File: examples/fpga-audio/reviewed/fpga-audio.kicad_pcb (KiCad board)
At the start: 2 copper layers, 100 x 84 mm, 29 parts, among them J1 3V3 IN, J2 AUDIO OUT, J3 SPI PROG, U1 iCE40UP5K, U2 PCM5102A, U3 AP2112K-1.2, U4 W25Q32JV, X1 12MHz

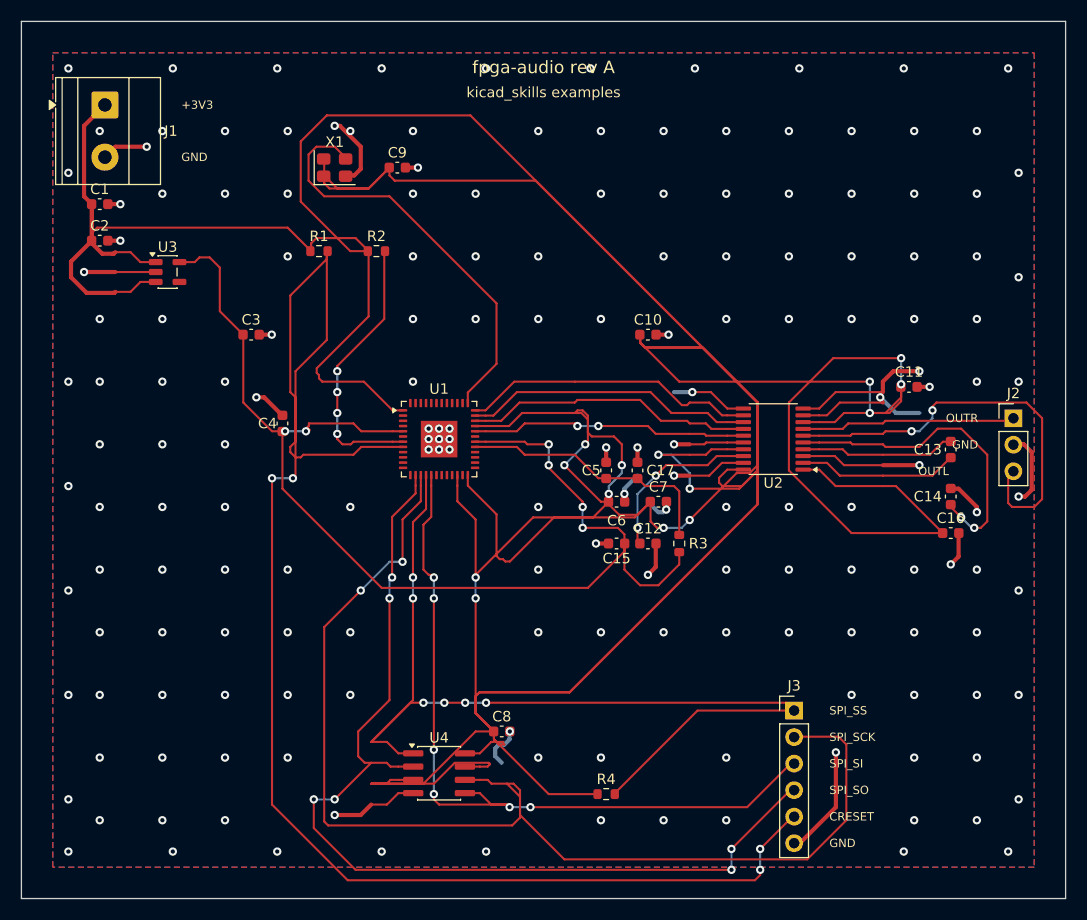
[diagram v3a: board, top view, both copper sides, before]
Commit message: Learn the drawing from the boards people drew
The brief for this round: relying on the autorouter and the numbers alone is
not enough - organise what pictorial correctness looks like from ordinary
circuits and open designs, and improve the drawing itself. So it starts in
KiCad's own demo corpus, measured and looked at, and ends with the habits
pushed into the generator.

tools/board_signature.py (new) reduces "looks autorouted" to five numbers.
Hand-routed two-layer boards cluster tightly: 10-47% of copper on the second
face, median segments 1.8-3.5 mm, 9-25 corners per decimetre, 91-98% of them
45s, 0.3-16 vias per decimetre. Rendering interf_u beside our boards says the
same thing in one glance: a layer has a direction, a bus travels as a bundle,
a person covers an offset with the long straight and one diagonal.

Three habits, now in the generator:

* Router.route(follow=...): cells beside a sibling net's path are discounted,
  so a bus (nets sharing a name prefix - I2S_*, SPI_*) travels as parallel
  lanes in one corridor. The discount is a fraction of a step, so it never
  buys a detour.
* _doglegged: every wiggly stretch is redrawn as the human stroke - the
  straight along the dominant direction plus one 45 - when the dogleg is
  clear, recursing into halves where a crossing blocks the whole. The op-amp
  board's median segment rose from 0.75 mm and its corner rate fell from
  38/dm; the FPGA board landed at 1.54 mm and 17.8/dm, inside the human band.
* Purposeful stitching: the 6 mm via carpet is gone. A ring at the rim, vias
  beside every back-layer crossing (where the plane is actually cut), and a
  coarse 12 mm mesh so no pour orphans. Vias/dm: buck 41 -> 18, carrier
  28 -> 13, all five inside the corpus band, pour_fragmented still silent.

Three failures the round produced and what they taught:

* pinned(): reshaping may not move copper off any point inside an own-net
  pad - the centre alone was not enough, a routed run touches off-centre and
  the ove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
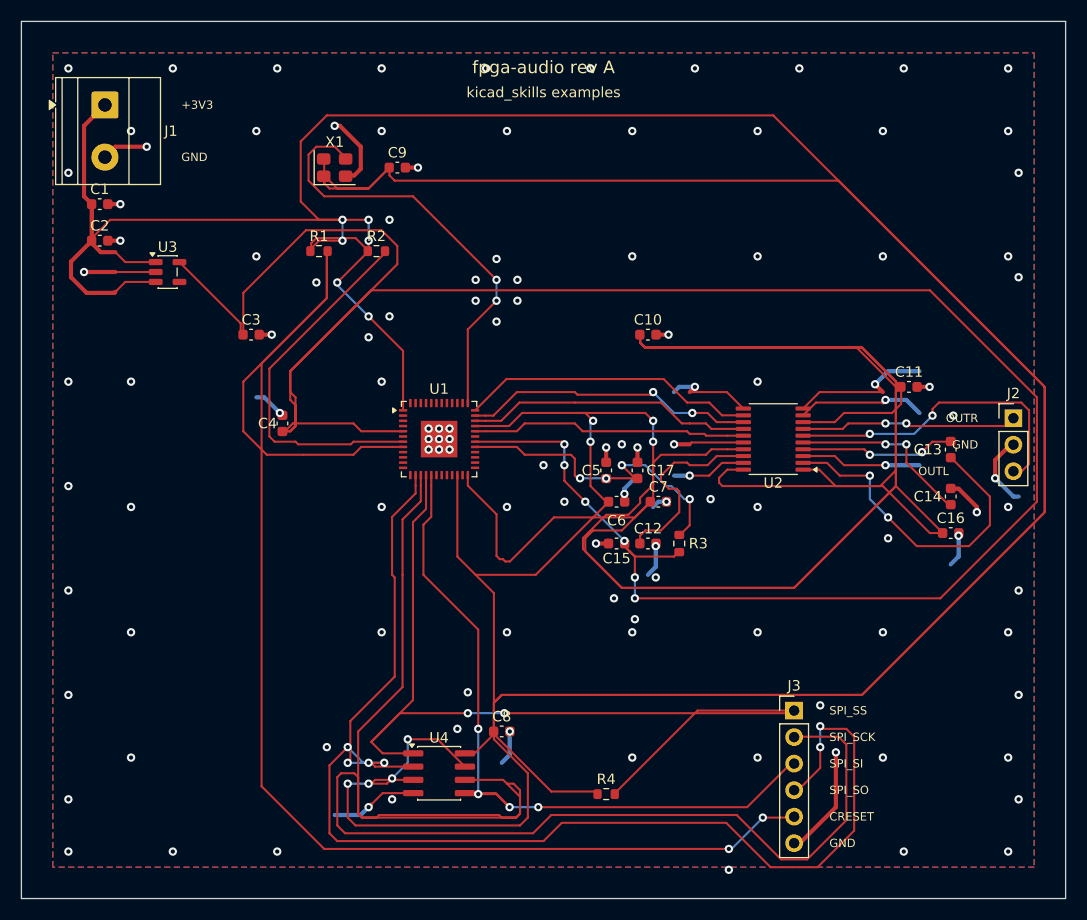
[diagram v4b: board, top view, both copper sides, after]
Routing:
- net +3V3: track 685.4 -> 905.9 mm
- net /+1V2: track 112.4 -> 237.2 mm
- net /SPI_SCK: track 115.9 -> 154.2 mm, vias 2 -> 0
- net /SPI_SO: track 96.7 -> 125.8 mm
- net /CAPP: track 15.4 -> 31.4 mm, vias 0 -> 2
- net /VNEG: track 30.8 -> 17.6 mm
- net /OUTL: track 40.2 -> 30.5 mm
- net /CDONE: track 26.5 -> 35.6 mm, vias 4 -> 0
- net /VCCPLL: track 25.5 -> 31.5 mm, vias 0 -> 4
- net /SPI_SI: track 73.2 -> 70.1 mm, vias 6 -> 4
- net /LDOO: track 16.5 -> 19.0 mm, vias 2 -> 0
- net /CLK12: track 40.5 -> 41.8 mm, vias 0 -> 2
- net /SPI_SS: track 95.1 -> 94.5 mm, vias 6 -> 2
- net /CRESET: track 146.0 -> 145.7 mm, vias 4 -> 2
- net GND: track 138.1 -> 137.8 mm, vias 177 -> 121
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
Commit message: A net may not cross its own copper
The reviewer looked at the plots, saw tracks driven through each other, and
asked whether the other checks were really passing. Both halves of the
answer were worth keeping. Measured directly - every pair of same-layer
segments on every reviewed board - there is not one crossing between
different nets: DRC reports zero errors, zero shorts, zero unconnected, and
it is not being fooled. What the plots show is a net crossing *itself*:
thirteen places on the FPGA board, one each on the op-amp and the buck.
Same potential, so DRC has nothing to say; no length ratio catches it; no
rule of ours looked. The checks were honest. The check list had a hole
exactly the shape of what the eye catches first.

route.self_crossing (new, warning, promoted by ai-generated) measures it:
two branches of one net crossing means the copper carries a redundant loop,
and a person never draws one. KiCad's demo corpus: 6 of 16 boards carry one
to three, at dense escapes.

_unlooped (new pass) is the fix, as a graph question: split every same-net
crossing so the X is a node, and while any cycle remains in the net's
copper, remove the longest junction-to-junction chain of the cycle -
connectivity is kept by definition, a cycle has two ways round, and the
amputated X becomes an ordinary corner. The clearance oracle now also
refuses to let _doglegged or _straighten draw a new X over their own net.

The cutter was wrong twice before it was right, both times the same lesson:
KiCad's connectivity is geometric, a track graph is endpoint topology, and
the difference is exactly a pad. The escape fan draws a micro-hook inside
an off-grid pad - the overlap is the connection - and the graph read it as
a dangling loop and amputated the pad's only feed. Nodes inside an own-net
pad are anchors now, a cycle wholly inside one pad is immune, and segments
passing over a pad are split so the feed is a node the cut must respect.

Self-crossings on the five reviewed boards: 0/0/0/0/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
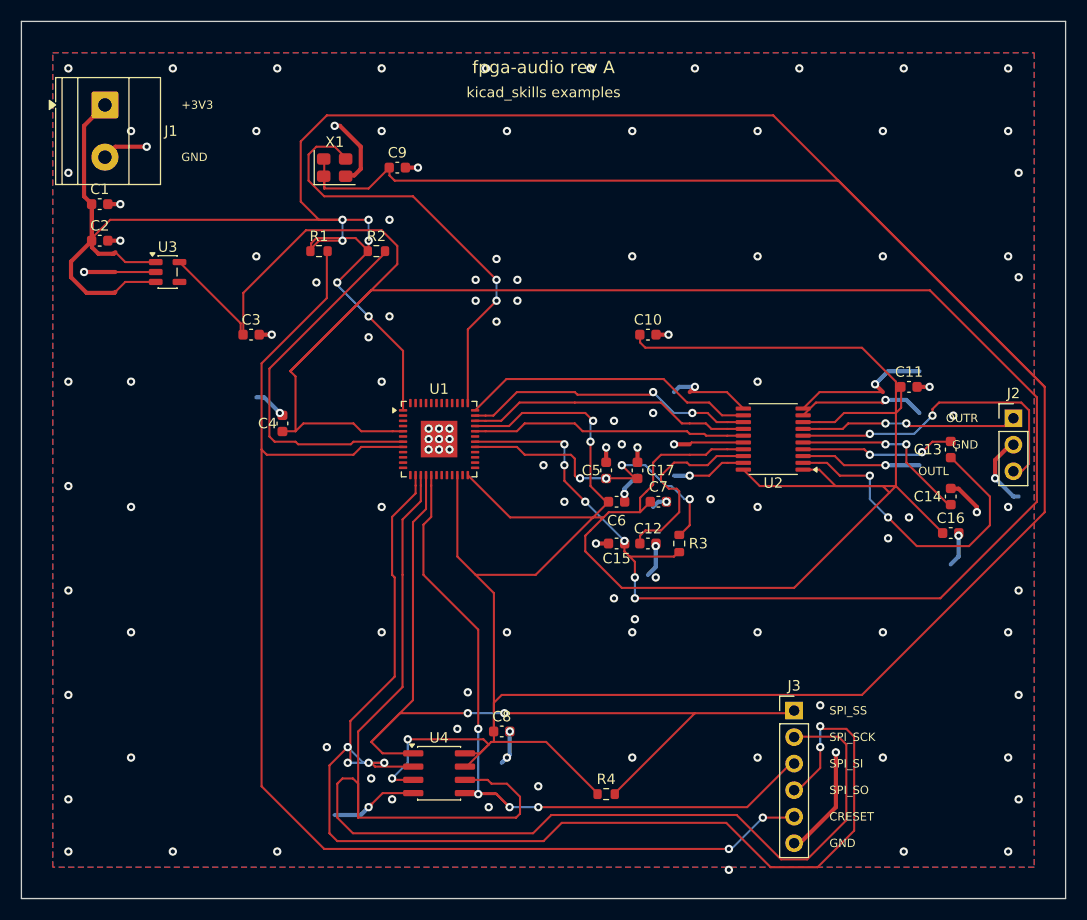
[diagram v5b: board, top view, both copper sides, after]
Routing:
- net +3V3: track 905.9 -> 603.0 mm, vias 14 -> 10
- net /CRESET: track 145.7 -> 122.9 mm
- net /SPI_SCK: track 154.2 -> 133.4 mm
- net /SPI_SS: track 94.5 -> 84.9 mm
- net /+1V2: track 237.2 -> 228.7 mm
- net GND: vias 121 -> 127

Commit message: Regenerate the FPGA board on the spine, and write round twelve down
The circled cluster is gone as a class: C15 is fed by one arm, junctions
sit on the trunks, and no small pad on any board carries more than three
arms - where the hand-routed corpus sits. The board is 15% lighter in
copper (1860 mm to 1583 mm). The rails no longer wander; what the gate
still blocks on is three SPI nets over plane cuts, two signal detours and
three corners - floorplan on a QFN-48 over two layers, stated rather than
waived. REVIEW.md section 17 records the round, including the three
check_board catches it took to state one straight stroke under a QFN.

Co-Authored-By: Claude Fable 5 <noreply@anthropic.com>
Claude-Session: https://claude.ai/code/session_01DUj7Ltu92tWg159mCSacwY
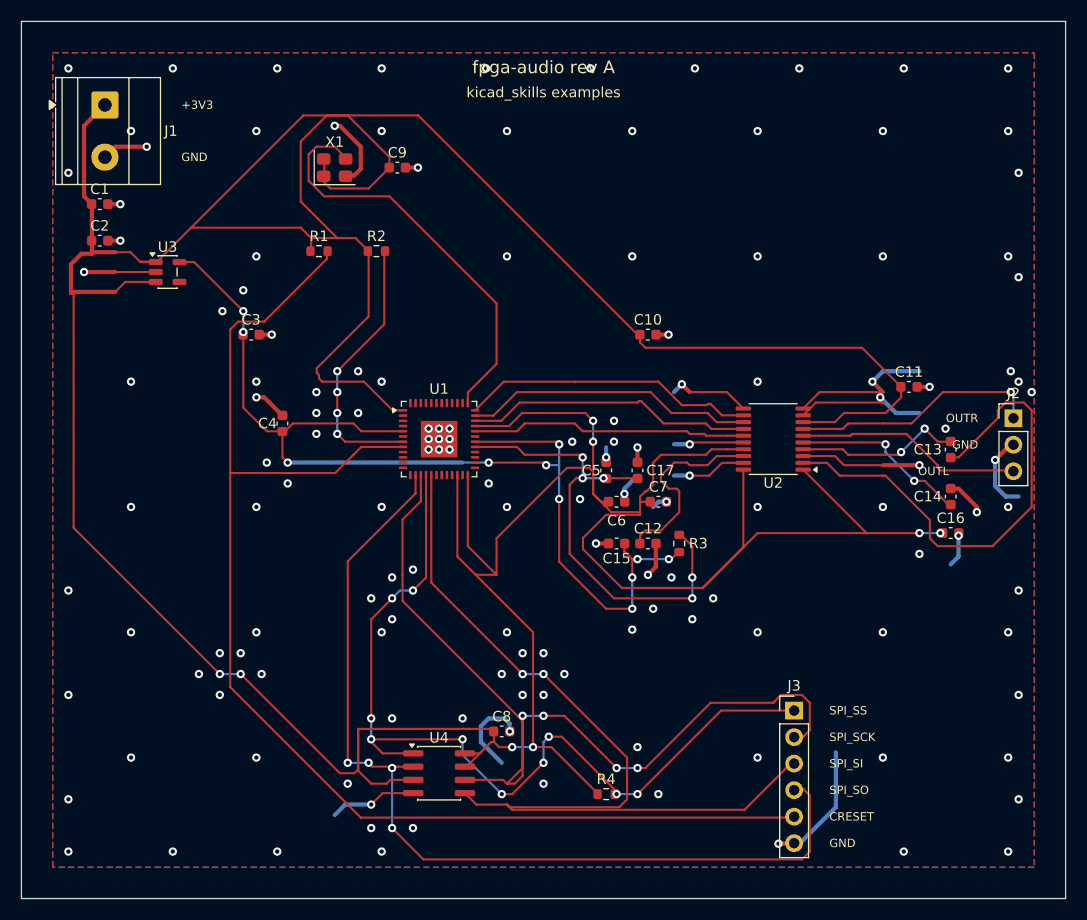
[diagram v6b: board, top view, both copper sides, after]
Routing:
- net /+1V2: track 228.7 -> 103.1 mm, vias 6 -> 11
- net +3V3: track 603.0 -> 492.9 mm, vias 10 -> 8
- net /SPI_SCK: track 133.4 -> 84.6 mm, vias 0 -> 4
- net /SPI_SO: track 125.8 -> 91.3 mm, vias 6 -> 4
- net /CAPP: track 31.4 -> 47.7 mm, vias 2 -> 0
- net /SPI_SI: track 70.1 -> 86.0 mm, vias 4 -> 2
- net /VCCPLL: track 31.5 -> 46.6 mm, vias 4 -> 5
- net /CDONE: track 35.6 -> 26.0 mm, vias 0 -> 4
- net GND: track 137.8 -> 146.8 mm, vias 127 -> 146
- net /OUTL: track 30.5 -> 21.8 mm, vias 2 -> 0
- net /OUTR: track 20.8 -> 24.0 mm, vias 2 -> 1
- net /CLK12: track 41.8 -> 40.5 mm, vias 2 -> 0
- net /SPI_SS: track 84.9 -> 86.0 mm, vias 2 -> 10
- net /CAPM: track 14.9 -> 15.9 mm
- net /CRESET: track 122.9 -> 123.9 mm, vias 2 -> 0
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
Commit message: Regenerate all five on the round-thirteen rules, and write the round down
The four fast boards pass their gates; measured across all five there are
zero crossings, zero doubled runs, zero mid-run width steps, every pour
piece over 8 mm2 holds its own via, and the shell reaches to 1.2 mm of
every edge. The FPGA sheet's two power blocks move clear of the frame -
the extended margin rule caught the second one this round. Its board
still fails, and the debt now has one name: four SPI nets at 11-20 mm
over plane cuts, two corners, and three detours all on the 3.3 V rail,
the twenty-link net that wants the same stated spine the 1.2 V rail got.
REVIEW.md section 18 records the round.

Co-Authored-By: Claude Fable 5 <noreply@anthropic.com>
Claude-Session: https://claude.ai/code/session_01DUj7Ltu92tWg159mCSacwY
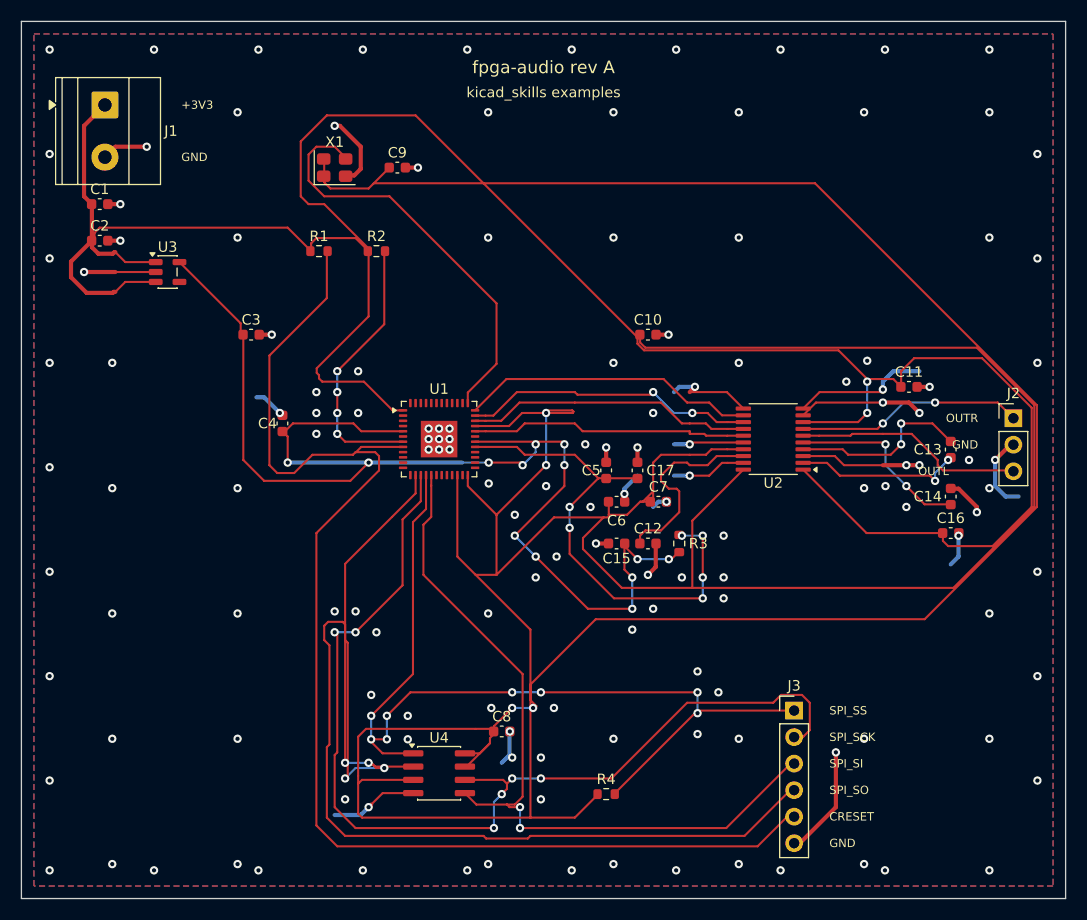
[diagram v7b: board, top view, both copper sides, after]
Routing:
- net +3V3: track 492.9 -> 670.7 mm, vias 8 -> 6
- net /SPI_SO: track 91.3 -> 126.1 mm
- net /CAPP: track 47.7 -> 16.2 mm, vias 0 -> 2
- net /+1V2: track 103.1 -> 121.9 mm, vias 11 -> 13
- net /SPI_SCK: track 84.6 -> 98.9 mm, vias 4 -> 6
- net /SPI_SI: track 86.0 -> 73.6 mm
- net GND: track 146.8 -> 137.1 mm, vias 146 -> 145
- net /SPI_SS: track 86.0 -> 89.5 mm, vias 10 -> 8
- net /OUTR: track 24.0 -> 21.8 mm, vias 1 -> 2
- net /CAPM: track 15.9 -> 17.5 mm
- net /VCCPLL: track 46.6 -> 48.0 mm, vias 5 -> 6
- net /CRESET: track 123.9 -> 124.9 mm
- net /VNEG: track 17.0 -> 17.8 mm
- net /I2S_BCK: track 27.8 -> 28.0 mm, vias 0 -> 2
